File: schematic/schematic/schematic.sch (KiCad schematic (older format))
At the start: 105 parts, among them J1 USB_A, J10 Conn_Tale, J2 USB_B_Micro, J3 Conn_PWM0, J4 Conn_PWM1, J5 Conn_SPI, J6 Conn_I2C, J7 Conn_GPIO, J8 Conn_Tale, J9 Conn_M5StickV, M1 Motor_DC, Q1 SS8050, Q2 SS8050, Q3 IRLML6402, Q4 PJE260N02, Q5 IRLML6402, Q6 PJE260N02, Q7 PJE260N02, SW1 SW_EN, SW2 SW_IO0, SW3 PS-85N, U1 TPS63002, U2 TPS63001, U3 MCP73831-5-OT, U4 FT231XS, U5 DW01-P, U6 BR8205, U7 TB6612FNG, U8 ESP32-WROOM-32D

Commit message: wip: add another layer
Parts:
- J1: footprint (none) -> micelib:USB_A_Vertical
- J2: footprint (none) -> Connector_USB:USB_Micro-B_Molex-105133-0001
- R1, R10, R12, R13, R14, R15, R16, R17, R18, R19, R2, R20, R21, R22, R23, R24, R25, R26, R3, R30, R31, R32, R33, R4, R6, R7, R8, R9: footprint (none) -> micelib:C_0402_1005Metric_HandSoldering
- R5: footprint (none) -> Resistor_SMD:R_1206_3216Metric_Pad1.42x1.75mm_HandSolder
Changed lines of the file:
@@
 F 0 "R12" H 5959 7446 50  0000 L CNN
 F 1 "10k" H 5959 7355 50  0000 L CNN
-F 2 "" H 5900 7400 50  0001 C CNN
+F 2 "micelib:C_0402_1005Metric_HandSoldering" H 5900 7400 50  0001 C CNN
 F 3 "~" H 5900 7400 50  0001 C CNN
 	1    5900 7400
@@
 F 0 "J2" H 550 6200 50  0000 C CNN
 F 1 "USB_B_Micro" H 950 6200 50  0000 C CNN
-F 2 "" H 900 5800 50  0001 C CNN
+F 2 "Connector_USB:USB_Micro-B_Molex-105133-0001" H 900 5800 50  0001 C CNN
 F 3 "~" H 900 5800 50  0001 C CNN
 	1    750  5850
@@
 F 0 "R1" H 1659 6296 50  0000 L CNN
 F 1 "10k" H 1659 6205 50  0000 L CNN
-F 2 "" H 1600 6250 50  0001 C CNN
+F 2 "micelib:C_0402_1005Metric_HandSoldering" H 1600 6250 50  0001 C CNN
 F 3 "~" H 1600 6250 50  0001 C CNN
 	1    1600 6250
@@
 F 0 "R22" H 8009 1196 50  0000 L CNN
 F 1 "1k" H 8009 1105 50  0000 L CNN
-F 2 "" H 7950 1150 50  0001 C CNN
+F 2 "micelib:C_0402_1005Metric_HandSoldering" H 7950 1150 50  0001 C CNN
 F 3 "~" H 7950 1150 50  0001 C CNN
 	1    7950 1150
@@
 F 0 "R8" V 5450 5550 50  0000 C CNN
 F 1 "100k" V 5550 5550 50  0000 C CNN
-F 2 "" H 5650 5550 50  0001 C CNN
+F 2 "micelib:C_0402_1005Metric_HandSoldering" H 5650 5550 50  0001 C CNN
 F 3 "~" H 5650 5550 50  0001 C CNN
 	1    5650 5550
@@
 F 0 "R2" V 3354 5850 50  0000 C CNN
 F 1 "100" V 3445 5850 50  0000 C CNN
-F 2 "" H 3550 5850 50  0001 C CNN
+F 2 "micelib:C_0402_1005Metric_HandSoldering" H 3550 5850 50  0001 C CNN
 F 3 "~" H 3550 5850 50  0001 C CNN
 	1    3550 5850
@@
 F 0 "R7" H 4900 6350 50  0000 L CNN
 F 1 "1k" H 4900 6250 50  0000 L CNN
-F 2 "" H 5050 6300 50  0001 C CNN
+F 2 "micelib:C_0402_1005Metric_HandSoldering" H 5050 6300 50  0001 C CNN
 F 3 "~" H 5050 6300 50  0001 C CNN
 	1    5050 6300
@@
 F 0 "R5" V 4554 6450 50  0000 C CNN
 F 1 "0.1" V 4645 6450 50  0000 C CNN
-F 2 "" H 4750 6450 50  0001 C CNN
+F 2 "Resistor_SMD:R_1206_3216Metric_Pad1.42x1.75mm_HandSolder" H 4750 6450 50  0001 C CNN
 F 3 "~" H 4750 6450 50  0001 C CNN
 	1    4750 6450
@@
 F 0 "R25" H 8709 1296 50  0000 L CNN
 F 1 "10k" H 8709 1205 50  0000 L CNN
-F 2 "" H 8650 1250 50  0001 C CNN
+F 2 "micelib:C_0402_1005Metric_HandSoldering" H 8650 1250 50  0001 C CNN
 F 3 "~" H 8650 1250 50  0001 C CNN
 	1    8650 1250
@@
 F 0 "R31" V 10604 1650 50  0000 C CNN
 F 1 "10k" V 10695 1650 50  0000 C CNN
-F 2 "" H 10800 1650 50  0001 C CNN
+F 2 "micelib:C_0402_1005Metric_HandSoldering" H 10800 1650 50  0001 C CNN
 F 3 "~" H 10800 1650 50  0001 C CNN
 	1    10800 1650
@@
 F 0 "R30" H 10409 1296 50  0000 L CNN
 F 1 "10k" H 10409 1205 50  0000 L CNN
-F 2 "" H 10350 1250 50  0001 C CNN
+F 2 "micelib:C_0402_1005Metric_HandSoldering" H 10350 1250 50  0001 C CNN
 F 3 "~" H 10350 1250 50  0001 C CNN
 	1    10350 1250
@@
 F 0 "R3" V 4354 1000 50  0000 C CNN
 F 1 "10k" V 4445 1000 50  0000 C CNN
-F 2 "" H 4550 1000 50  0001 C CNN
+F 2 "micelib:C_0402_1005Metric_HandSoldering" H 4550 1000 50  0001 C CNN
 F 3 "~" H 4550 1000 50  0001 C CNN
 	1    4550 1000
@@
 F 0 "R4" V 4354 1650 50  0000 C CNN
 F 1 "10k" V 4445 1650 50  0000 C CNN
-F 2 "" H 4550 1650 50  0001 C CNN
+F 2 "micelib:C_0402_1005Metric_HandSoldering" H 4550 1650 50  0001 C CNN
 F 3 "~" H 4550 1650 50  0001 C CNN
 	1    4550 1650
@@
 F 0 "R19" H 7209 1346 50  0000 L CNN
 F 1 "1k" H 7209 1255 50  0000 L CNN
-F 2 "" H 7150 1300 50  0001 C CNN
+F 2 "micelib:C_0402_1005Metric_HandSoldering" H 7150 1300 50  0001 C CNN
 F 3 "~" H 7150 1300 50  0001 C CNN
 	1    7150 1300
@@
 F 0 "R13" H 6209 1146 50  0000 L CNN
 F 1 "1k" H 6209 1055 50  0000 L CNN
-F 2 "" H 6150 1100 50  0001 C CNN
+F 2 "micelib:C_0402_1005Metric_HandSoldering" H 6150 1100 50  0001 C CNN
 F 3 "~" H 6150 1100 50  0001 C CNN
 	1    6150 1100
@@
 F 0 "R6" V 4654 2350 50  0000 C CNN
 F 1 "470" V 4745 2350 50  0000 C CNN
-F 2 "" H 4850 2350 50  0001 C CNN
+F 2 "micelib:C_0402_1005Metric_HandSoldering" H 4850 2350 50  0001 C CNN
 F 3 "~" H 4850 2350 50  0001 C CNN
 	1    4850 2350
@@
 F 0 "R17" H 6459 2196 50  0000 L CNN
 F 1 "2.2k" H 6459 2105 50  0000 L CNN
-F 2 "" H 6400 2150 50  0001 C CNN
+F 2 "micelib:C_0402_1005Metric_HandSoldering" H 6400 2150 50  0001 C CNN
 F 3 "~" H 6400 2150 50  0001 C CNN
 	1    6400 2150
@@
 F 0 "R14" H 6209 1346 50  0000 L CNN
 F 1 "1k" H 6209 1255 50  0000 L CNN
-F 2 "" H 6150 1300 50  0001 C CNN
+F 2 "micelib:C_0402_1005Metric_HandSoldering" H 6150 1300 50  0001 C CNN
 F 3 "~" H 6150 1300 50  0001 C CNN
 	1    6150 1300
@@
 F 0 "R10" H 5859 3246 50  0000 L CNN
 F 1 "1k" H 5859 3155 50  0000 L CNN
-F 2 "" H 5800 3200 50  0001 C CNN
+F 2 "micelib:C_0402_1005Metric_HandSoldering" H 5800 3200 50  0001 C CNN
 F 3 "~" H 5800 3200 50  0001 C CNN
 	1    5800 3200
@@
 F 0 "R16" H 6409 3246 50  0000 L CNN
 F 1 "1k" H 6409 3155 50  0000 L CNN
-F 2 "" H 6350 3200 50  0001 C CNN
+F 2 "micelib:C_0402_1005Metric_HandSoldering" H 6350 3200 50  0001 C CNN
 F 3 "~" H 6350 3200 50  0001 C CNN
 	1    6350 3200
@@
 F 0 "R15" H 6209 3796 50  0000 L CNN
 F 1 "100k" H 6209 3705 50  0000 L CNN
-F 2 "" H 6150 3750 50  0001 C CNN
+F 2 "micelib:C_0402_1005Metric_HandSoldering" H 6150 3750 50  0001 C CNN
 F 3 "~" H 6150 3750 50  0001 C CNN
 	1    6150 3750
@@
 F 0 "R18" H 6959 3146 50  0000 L CNN
 F 1 "1k" H 6959 3055 50  0000 L CNN
-F 2 "" H 6900 3100 50  0001 C CNN
+F 2 "micelib:C_0402_1005Metric_HandSoldering" H 6900 3100 50  0001 C CNN
 F 3 "~" H 6900 3100 50  0001 C CNN
 	1    6900 3100
@@
 F 0 "R20" H 7309 3696 50  0000 L CNN
 F 1 "100k" H 7309 3605 50  0000 L CNN
-F 2 "" H 7250 3650 50  0001 C CNN
+F 2 "micelib:C_0402_1005Metric_HandSoldering" H 7250 3650 50  0001 C CNN
 F 3 "~" H 7250 3650 50  0001 C CNN
 	1    7250 3650
@@
 F 0 "R23" H 8059 2096 50  0000 L CNN
 F 1 "1k" H 8059 2005 50  0000 L CNN
-F 2 "" H 8000 2050 50  0001 C CNN
+F 2 "micelib:C_0402_1005Metric_HandSoldering" H 8000 2050 50  0001 C CNN
 F 3 "~" H 8000 2050 50  0001 C CNN
 	1    8000 2050
@@
 F 0 "R21" H 7709 2646 50  0000 L CNN
 F 1 "100k" H 7709 2555 50  0000 L CNN
-F 2 "" H 7650 2600 50  0001 C CNN
+F 2 "micelib:C_0402_1005Metric_HandSoldering" H 7650 2600 50  0001 C CNN
 F 3 "~" H 7650 2600 50  0001 C CNN
 	1    7650 2600
@@
 F 0 "R26" H 8709 3946 50  0000 L CNN
 F 1 "10k" H 8709 3855 50  0000 L CNN
-F 2 "" H 8650 3900 50  0001 C CNN
+F 2 "micelib:C_0402_1005Metric_HandSoldering" H 8650 3900 50  0001 C CNN
 F 3 "~" H 8650 3900 50  0001 C CNN
 	1    8650 3900
@@
 F 0 "R24" H 8491 3854 50  0000 R CNN
 F 1 "10k" H 8491 3945 50  0000 R CNN
-F 2 "" H 8550 3900 50  0001 C CNN
+F 2 "micelib:C_0402_1005Metric_HandSoldering" H 8550 3900 50  0001 C CNN
 F 3 "~" H 8550 3900 50  0001 C CNN
 	1    8550 3900
@@
 F 0 "J1" H 650 4150 50  0000 C CNN
 F 1 "USB_A" H 650 4050 50  0000 C CNN
-F 2 "" H 900 4600 50  0001 C CNN
+F 2 "micelib:USB_A_Vertical" H 900 4600 50  0001 C CNN
 F 3 " ~" H 900 4600 50  0001 C CNN
 	1    750  4650
@@
 F 0 "R9" H 5600 7650 50  0000 L CNN
 F 1 "47" H 5550 7550 50  0000 L CNN
-F 2 "" H 5750 7600 50  0001 C CNN
+F 2 "micelib:C_0402_1005Metric_HandSoldering" H 5750 7600 50  0001 C CNN
 F 3 "~" H 5750 7600 50  0001 C CNN
 	1    5750 7600
@@
 F 0 "R32" H 3409 6996 50  0000 L CNN
 F 1 "10k" H 3409 6905 50  0000 L CNN
-F 2 "" H 3350 6950 50  0001 C CNN
+F 2 "micelib:C_0402_1005Metric_HandSoldering" H 3350 6950 50  0001 C CNN
 F 3 "~" H 3350 6950 50  0001 C CNN
 	1    3350 6950
@@
 F 0 "R33" H 3409 7296 50  0000 L CNN
 F 1 "10k" H 3409 7205 50  0000 L CNN
-F 2 "" H 3350 7250 50  0001 C CNN
+F 2 "micelib:C_0402_1005Metric_HandSoldering" H 3350 7250 50  0001 C CNN
 F 3 "~" H 3350 7250 50  0001 C CNN
 	1    3350 7250

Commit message: 配置開始
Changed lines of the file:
@@
 Connection ~ 2950 4850
-$Comp
-L power:GND #PWR029
-U 1 1 5E5CB358
-P 3600 5100
-F 0 "#PWR029" H 3600 4850 50  0001 C CNN
-F 1 "GND" H 3600 4950 50  0000 C CNN
-F 2 "" H 3600 5100 50  0001 C CNN
-F 3 "" H 3600 5100 50  0001 C CNN
-	1    3600 5100
-	1    0    0    -1
-$EndComp
 $Comp
 L power:GNDD #PWR035
@@
 	2850 600  11100 600
 Wire Notes Line
-	500  4300 11100 4300
-Wire Notes Line
 	8300 600  8300 4300
 $Comp
@@
 P 7900 4650
 F 0 "#PWR051" H 7900 4500 50  0001 C CNN
-F 1 "+3V3" H 7915 4823 50  0000 C CNN
+F 1 "+3V3" H 7900 4800 50  0000 C CNN
 F 2 "" H 7900 4650 50  0001 C CNN
 F 3 "" H 7900 4650 50  0001 C CNN
@@
 	5950 1300 6050 1300
 $Sheet
-S 10100 5900 1000 450
+S 10000 6000 1000 450
 U 5E247314
 F0 "Sensors" 50
@@
 	9550 5000 10150 5000
 Connection ~ 9550 5000
+Wire Notes Line
+	150  4300 11100 4300
+$Comp
+L power:GNDD #PWR029
+U 1 1 5E5B182E
+P 3600 5100
+F 0 "#PWR029" H 3600 4850 50  0001 C CNN
+F 1 "GNDD" H 3604 4945 50  0000 C CNN
+F 2 "" H 3600 5100 50  0001 C CNN
+F 3 "" H 3600 5100 50  0001 C CNN
+	1    3600 5100
+	1    0    0    -1
+$EndComp
 $EndSCHEMATC

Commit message: Pin Assign test
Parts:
- U1: footprint Connector_PinHeader_2.54mm:PinHeader_1x05_P2.54mm_Vertical -> micelib:WSON-10-1EP_2x3mm_P0.5mm_EP0.84x2.4mm_TPS6300x
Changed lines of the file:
@@
 F 0 "U1" H 1600 3865 50  0000 C CNN
 F 1 "TPS63002" H 1600 3774 50  0000 C CNN
-F 2 "Connector_PinHeader_2.54mm:PinHeader_1x05_P2.54mm_Vertical" H 1600 3400 50  0001 C CNN
+F 2 "micelib:WSON-10-1EP_2x3mm_P0.5mm_EP0.84x2.4mm_TPS6300x" H 1600 3400 50  0001 C CNN
 F 3 "" H 1600 3400 50  0001 C CNN
 	1    1600 3400

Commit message: 地獄の配線
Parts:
- removed C14, C26, C8: 0.1u, micelib:C_0402_1005Metric_HandSoldering, symbol Device:C_Small
- removed C16: 4.7u, micelib:C_0402_1005Metric_HandSoldering, symbol Device:C_Small
- removed C4, C5: 10u, Capacitor_SMD:C_0603_1608Metric_Pad1.05x0.95mm_HandSolder, symbol Device:C_Small
- removed D1: SS2040FL, Diode_SMD:D_SOD-123F, symbol Device:D_Schottky_Small
- removed J1: USB_A, micelib:USB_A_Vertical, symbol Connector:USB_A
- removed J3: Conn_PWM0, Connector_PinHeader_2.54mm:PinHeader_1x03_P2.54mm_Vertical, symbol Connector_Generic:Conn_01x03
- removed J4: Conn_PWM1, Connector_PinHeader_2.54mm:PinHeader_1x03_P2.54mm_Vertical, symbol Connector_Generic:Conn_01x03
- removed J5: Conn_SPI, Connector_PinHeader_2.54mm:PinHeader_1x05_P2.54mm_Vertical, symbol Connector_Generic:Conn_01x05
- removed J7: Conn_GPIO, Connector_PinHeader_2.54mm:PinHeader_1x02_P2.54mm_Vertical, symbol Connector_Generic:Conn_01x02
- removed JP2: Jumper, Jumper:SolderJumper-2_P1.3mm_Bridged2Bar_Pad1.0x1.5mm, symbol Device:Jumper_NC_Small
- removed SW3: PS-85N, micelib:PS-85, symbol micelib:PS-85N
- removed TP1: 5V, Connector_PinHeader_1.27mm:PinHeader_1x01_P1.27mm_Vertical, symbol Connector:TestPoint
- removed TP2: 3.3V, Connector_PinHeader_1.27mm:PinHeader_1x01_P1.27mm_Vertical, symbol Connector:TestPoint
- removed TP3: +VBAT, Connector_PinHeader_1.27mm:PinHeader_1x01_P1.27mm_Vertical, symbol Connector:TestPoint
- added J3: Conn_02x03_Odd_Even, Connector_PinSocket_2.54mm:PinSocket_2x03_P2.54mm_Vertical, symbol Connector_Generic:Conn_02x03_Odd_Even
- added SW3: SW_SPDT, Connector_PinSocket_2.54mm:PinSocket_1x03_P2.54mm_Vertical, symbol Switch:SW_SPDT
- R15, R20, R21: value 100k -> 10k
- U8: footprint RF_Module:ESP32-WROOM-32 -> micelib:ESP32-WROOM-32_Hand
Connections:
- net labels removed: GPIO34, GPIO35
- wire segments 520 -> 467
- no-connect marks 28 -> 27
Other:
- note added: "I2C"
- note removed: "M5_Power"
- note removed: "SPI\n&\nI2C"
- moved on the sheet: C11, C12

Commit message: 一歩進んで仕様決めなおし
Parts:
- removed C15, C19, C20: 0.1u, micelib:C_0402_1005Metric_HandSoldering, symbol Device:C_Small
- removed C17: 47u, Capacitor_SMD:C_1210_3225Metric_Pad1.42x2.65mm_HandSolder, symbol Device:CP_Small
- removed C18: 10u, Capacitor_SMD:C_0603_1608Metric_Pad1.05x0.95mm_HandSolder, symbol Device:CP_Small
- removed J6: Conn_I2C, Connector_PinHeader_2.54mm:PinHeader_1x04_P2.54mm_Vertical, symbol Connector_Generic:Conn_01x04
- removed M1: Motor_DC, Connector_PinHeader_2.54mm:PinHeader_1x02_P2.54mm_Vertical, symbol Motor:Motor_DC
- removed U7: TB6612FNG, Package_SO:SSOP-24_5.3x8.2mm_P0.65mm, symbol Driver_Motor:TB6612FNG
- added IC?: DRV8830, symbol micelib:DRV8830
- added J?: Conn_GPIO, symbol Connector_Generic:Conn_01x03
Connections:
- net GPIO_33: now reaches U8.9 (IO33)
- net GPIO_33: now also J?.3 (Pin_3)
- net VSPI_CS0 renamed GPIO_5
- net GPIO_5: now also J?.1 (Pin_1)
- net VSPI_CS1 renamed GPIO_12
- net GPIO_12: now also J?.2 (Pin_2)
- no-connect marks 27 -> 19
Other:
- note added: "GPIO"
- note removed: "I2C"

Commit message: ちょっとシンプルにしよう
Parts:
- removed TP6: GND, Connector_PinHeader_1.27mm:PinHeader_1x01_P1.27mm_Vertical, symbol Connector:TestPoint
- added C12: 0.1u, symbol Device:C_Small
- added C13: 10u, symbol Device:C_Small
- added D7: LED_MD, LED_SMD:LED_0603_1608Metric_Pad1.05x0.95mm_HandSolder, symbol Device:LED_Small
- added M1: M_Small, symbol micelib:M_Small
- added Q7, Q8: BSS138, digikey-footprints:SOT-23-3, symbol dk_Transistors-FETs-MOSFETs-Single:BSS138
- added R20: 2.2k, micelib:C_0402_1005Metric_HandSoldering, symbol Device:R_Small
- added R26, R27, R?: 10k, symbol Device:R_Small
- added TP1: VBAT, Connector_PinHeader_1.27mm:PinHeader_1x01_P1.27mm_Vertical, symbol Connector:TestPoint
- gave numbers to parts that had none: 2
- renumbered C27 to C10, C13 to C11, C21 to C14, C25 to C15, C23 to C16, C24 to C17, C6 to C4, C7 to C5, C9 to C6, C10 to C7, C11 to C8, C12 to C9, D2 to D1, D4 to D2, D5 to D3, D6 to D4, D7 to D5, D8 to D6, D9 to D8, D10 to D9, J2 to J1, J3 to J2, J9 to J4, J10 to J5, J8 to J6, Q7 to Q9, R8 to R10, R9 to R11, R10 to R12, R12 to R13, R13 to R14, R14 to R15, R15 to R16, R16 to R17, R17 to R18, R18 to R19, R32 to R2, R19 to R21, R20 to R22, R21 to R23, R22 to R24, R23 to R25, R24 to R28, R25 to R29, R33 to R3, R26 to R30, R30 to R31, R31 to R32, R2 to R4, R3 to R5, R4 to R6, R5 to R7, R6 to R8, R7 to R9, TP4 to TP2, TP5 to TP3, U8 to U7
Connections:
- net +3V3: now also Q7.1 (G), Q8.1 (G)
- net +5V: now also D7.2 (A), R26.2, R27.1
- net GND: now also IC1.11 (GND_pad), IC1.2 (ISENSE), IC1.5 (GND), IC1.7 (A0), IC1.8 (A1), C12.1, C13.1
- net GNDD: now also R?.1
- net GPIO_12: now also R?.2
- net I2C_SCL: now also Q8.2 (S)
- net I2C_SDA: now also Q7.2 (S)
- net LED_BRAKE: now also J5.2 (Pin_2), J6.2 (Pin_2); no longer J5.1 (Pin_1), J6.1 (Pin_1)
- net LED_LEFT: now also J5.1 (Pin_1), J6.1 (Pin_1); no longer J5.2 (Pin_2), J6.2 (Pin_2)
- net VBAT: now also TP1.1
- net at IC1.1 (OUT2): now also M1.1
- net I2C_SCL_5V: now reaches IC1.10 (SCL)
- net I2C_SCL_5V: now also Q8.3 (D), R27.2
- net at IC1.3 (OUT1): now also M1.2
- net MD_VM: now reaches IC1.4 (VCC)
- net MD_VM: now also C12.2, C13.2
- net FAULTn: now reaches IC1.6 (FAULTn)
- net FAULTn: now also R20.2
- net I2C_SDA_5V: now reaches IC1.9 (SDA)
- net I2C_SDA_5V: now also Q7.3 (D), R26.1
- net MD_IN1: no longer names the net of U7.8 (IO32)
- net MD_IN2: no longer names the net of U7.26 (IO4)
- net PWM_MD: no longer names the net of U7.12 (IO27)
- net VSPI_CLK renamed SPI_CLK
- net VSPI_MISO renamed SPI_MISO
- net VSPI_MOSI renamed SPI_MOSI
- new net: D7.1 (K), R20.1
- no-connect marks 19 -> 22
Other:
- moved on the sheet: IC1, J5, J6

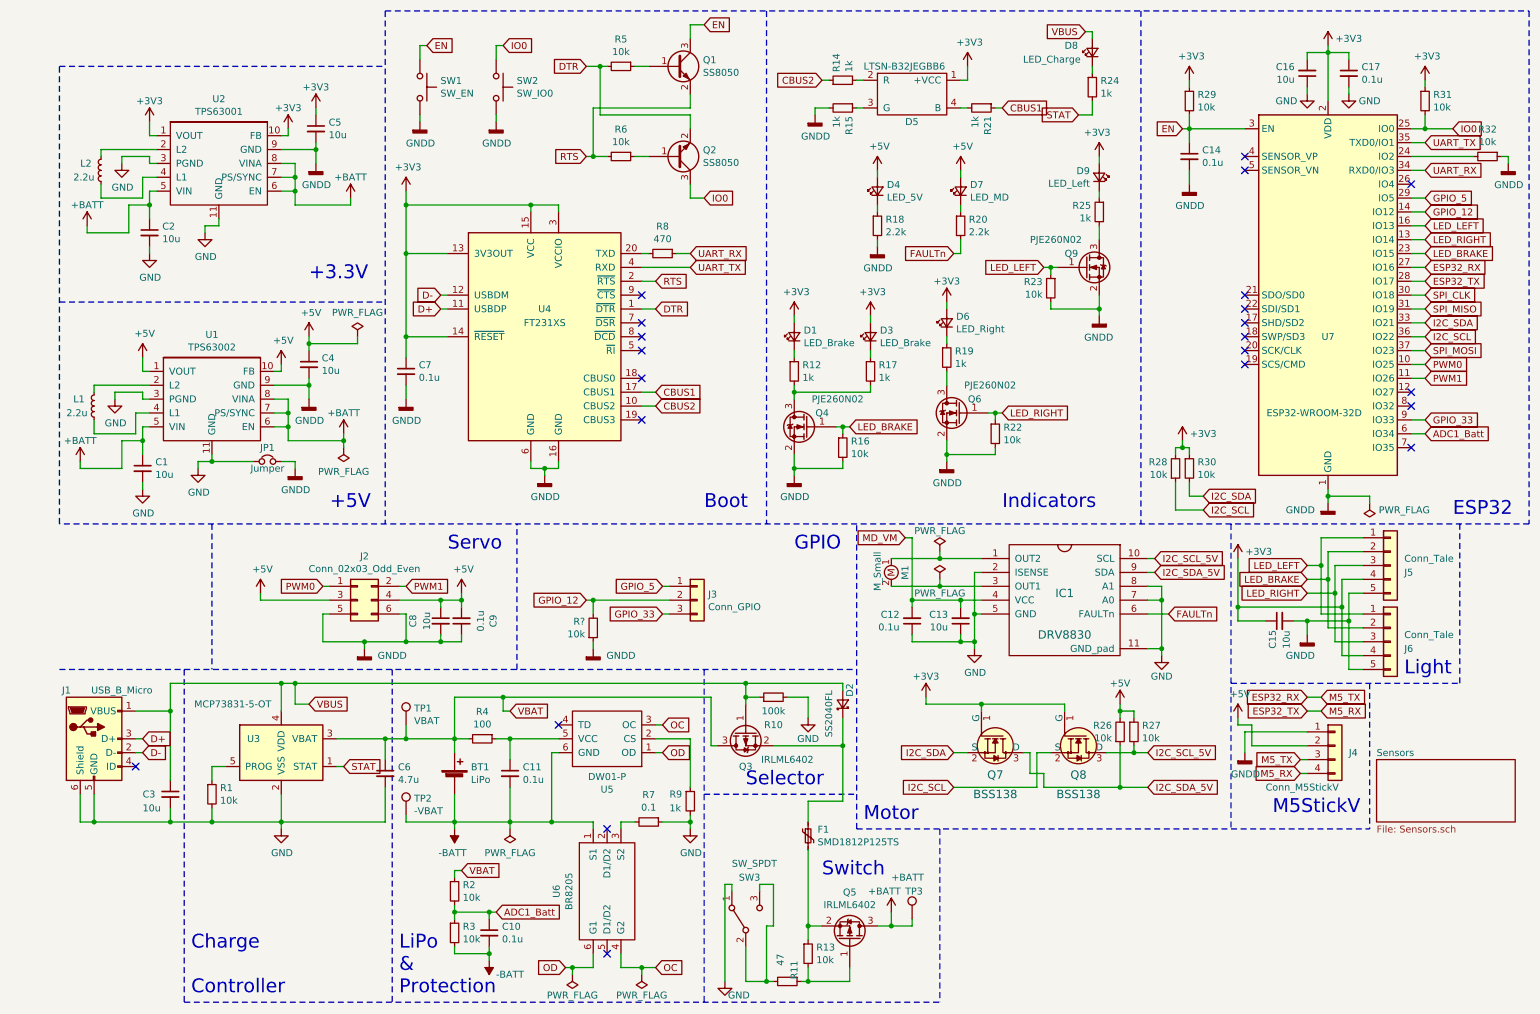
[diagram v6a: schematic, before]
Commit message: Change MD to DRV8830
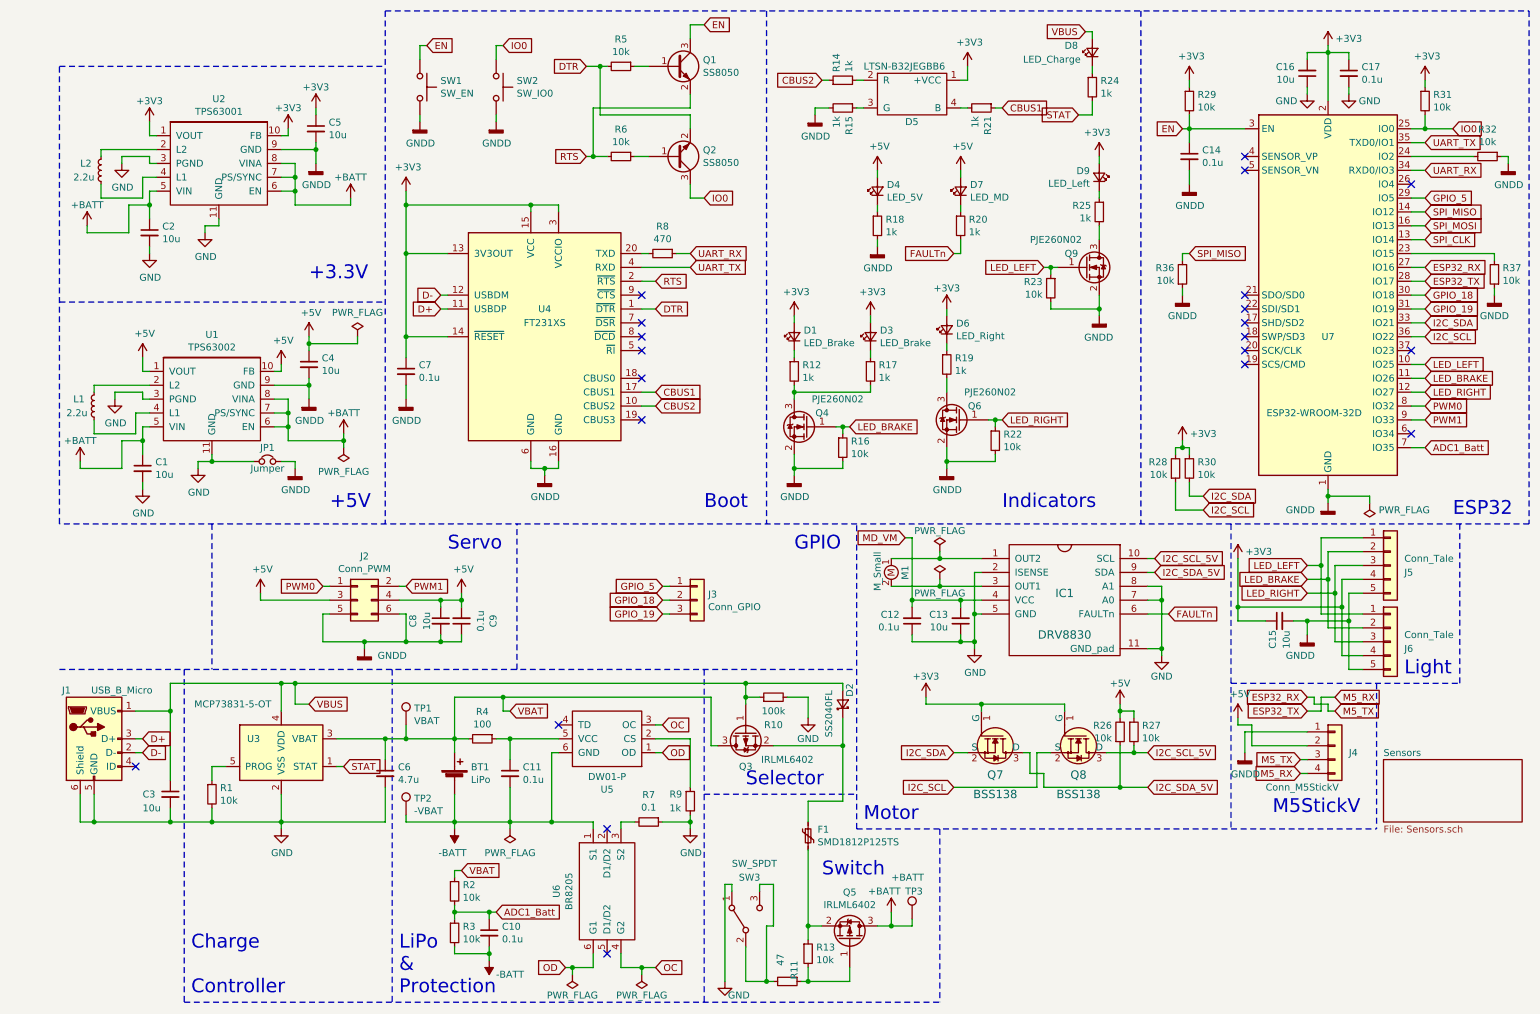
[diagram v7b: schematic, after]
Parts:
- removed R?: 10k, symbol Device:R_Small
- added R36, R37: 10k, micelib:C_0402_1005Metric_HandSoldering, symbol Device:R_Small
- C12, R26, R27: footprint (none) -> micelib:C_0402_1005Metric_HandSoldering
- C13: footprint (none) -> Capacitor_SMD:C_0603_1608Metric_Pad1.05x0.95mm_HandSolder
- IC1: footprint (none) -> micelib:MSOP-10-1EP_3x3mm_P0.5mm_EP1.68x1.88mm_DRV8830
- J2: value Conn_02x03_Odd_Even -> Conn_PWM
- J3: footprint (none) -> Connector_PinSocket_2.54mm:PinSocket_1x03_P2.54mm_Vertical
- M1: footprint (none) -> Connector_PinSocket_2.54mm:PinSocket_1x02_P2.54mm_Vertical
- Q7, Q8: footprint digikey-footprints:SOT-23-3 -> Package_TO_SOT_SMD:SOT-23
- R18, R20: value 2.2k -> 1k
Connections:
- net ADC1_Batt: now also U7.7 (IO35); no longer U7.6 (IO34)
- net GNDD: now also R36.1, R37.1
- net LED_BRAKE: now also U7.11 (IO26); no longer U7.23 (IO15)
- net LED_LEFT: now also U7.10 (IO25); no longer U7.16 (IO13)
- net LED_RIGHT: now also U7.12 (IO27); no longer U7.13 (IO14)
- net PWM0: now also U7.8 (IO32); no longer U7.10 (IO25)
- net PWM1: now also U7.9 (IO33); no longer U7.11 (IO26)
- net SPI_CLK: now also U7.13 (IO14); no longer U7.30 (IO18)
- net SPI_MISO: now also U7.14 (IO12), R36.2; no longer U7.31 (IO19)
- net SPI_MOSI: now also U7.16 (IO13); no longer U7.37 (IO23)
- net GPIO_12 renamed GPIO_18
- net GPIO_18: now also U7.30 (IO18); no longer U7.14 (IO12)
- net GPIO_33 renamed GPIO_19
- net GPIO_19: now also U7.31 (IO19); no longer U7.9 (IO33)
- new net: R37.2, U7.23 (IO15)
- no-connect marks 22 -> 21
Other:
- moved on the sheet: D6, Q6, R19, R22
